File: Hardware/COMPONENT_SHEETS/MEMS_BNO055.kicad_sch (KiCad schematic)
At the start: 6 parts, among them U8 BNO055, Y2 32.768kHz

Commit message: Added 3D models to components
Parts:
- Y2: footprint Crystal:Crystal_DS26_D2.0mm_L6.0mm_Horizontal_1EP_style2 -> RDT_Custom_Footprints:XTAL_ABM7-32.000MHZ-D2Y-T
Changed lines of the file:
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@@
       (effects (font (size 1.27 1.27)) (justify left))
     )
-    (property "Footprint" "Crystal:Crystal_DS26_D2.0mm_L6.0mm_Horizontal_1EP_style2" (id 2) (at 163.83 83.82 0)
+    (property "Footprint" "RDT_Custom_Footprints:XTAL_ABM7-32.000MHZ-D2Y-T" (id 2) (at 163.83 83.82 0)
       (effects (font (size 1.27 1.27)) hide)
     )

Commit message: Corrected PCB edge cuts, removed components
Will be mimicking layout done by Seth Sievers
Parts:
- renumbered C19 to C1, C20 to C2, C21 to C3, C22 to C4, U8 to U1, Y2 to Y1
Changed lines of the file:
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@@
   (symbol (lib_id "Data_Collection_KiCAD_Project-rescue:BNO055-Sensor_Motion-Data_Collection_KiCAD_Project-rescue") (at 143.51 90.17 0)
     (in_bom yes) (on_board yes)
-    (property "Reference" "U8" (id 0) (at 143.51 63.5 0))
+    (property "Reference" "U1" (id 0) (at 143.51 63.5 0))
     (property "Value" "BNO055" (id 1) (at 143.51 66.04 0))
     (property "Footprint" "Package_LGA:LGA-28_5.2x3.8mm_P0.5mm" (id 2) (at 149.86 106.68 0)
@@
   (symbol (lib_id "Data_Collection_KiCAD_Project-rescue:+3.3V-power-Data_Collection_KiCAD_Project-rescue") (at 132.08 68.58 0)
     (in_bom yes) (on_board yes)
-    (property "Reference" "#PWR042" (id 0) (at 132.08 72.39 0)
+    (property "Reference" "#PWR013" (id 0) (at 132.08 72.39 0)
       (effects (font (size 1.27 1.27)) hide)
     )
@@
   (symbol (lib_id "Data_Collection_KiCAD_Project-rescue:GND-power-Data_Collection_KiCAD_Project-rescue") (at 162.56 69.85 0) (unit 1)
     (in_bom yes) (on_board yes)
-    (property "Reference" "#PWR0102" (id 0) (at 162.56 76.2 0)
+    (property "Reference" "#PWR015" (id 0) (at 162.56 76.2 0)
       (effects (font (size 1.27 1.27)) hide)
     )
@@
   (symbol (lib_id "Data_Collection_KiCAD_Project-rescue:GND-power-Data_Collection_KiCAD_Project-rescue") (at 140.97 110.49 0) (unit 1)
     (in_bom yes) (on_board yes)
-    (property "Reference" "#PWR0103" (id 0) (at 140.97 116.84 0)
+    (property "Reference" "#PWR014" (id 0) (at 140.97 116.84 0)
       (effects (font (size 1.27 1.27)) hide)
     )
@@
   (symbol (lib_id "Data_Collection_KiCAD_Project-rescue:Crystal_Small-Device-Data_Collection_KiCAD_Project-rescue") (at 163.83 83.82 270) (unit 1)
     (in_bom yes) (on_board yes)
-    (property "Reference" "Y2" (id 0) (at 166.0652 82.6516 90)
+    (property "Reference" "Y1" (id 0) (at 166.0652 82.6516 90)
       (effects (font (size 1.27 1.27)) (justify left))
     )
@@
   (symbol (lib_id "Data_Collection_KiCAD_Project-rescue:C_Small-Device-Data_Collection_KiCAD_Project-rescue") (at 160.02 68.58 270)
     (in_bom yes) (on_board yes)
-    (property "Reference" "C19" (id 0) (at 160.02 62.7634 90))
+    (property "Reference" "C1" (id 0) (at 160.02 62.7634 90))
     (property "Value" "0.1uF" (id 1) (at 160.02 65.0748 90))
     (property "Footprint" "Capacitor_SMD:C_0603_1608Metric_Pad1.08x0.95mm_HandSolder" (id 2) (at 160.02 68.58 0)
@@
   (symbol (lib_id "Data_Collection_KiCAD_Project-rescue:C_Small-Device-Data_Collection_KiCAD_Project-rescue") (at 171.45 77.47 270)
     (in_bom yes) (on_board yes)
-    (property "Reference" "C21" (id 0) (at 171.45 71.6534 90))
+    (property "Reference" "C3" (id 0) (at 171.45 71.6534 90))
     (property "Value" "0.1uF" (id 1) (at 171.45 73.9648 90))
     (property "Footprint" "Capacitor_SMD:C_0603_1608Metric_Pad1.08x0.95mm_HandSolder" (id 2) (at 171.45 77.47 0)
@@
   (symbol (lib_id "Data_Collection_KiCAD_Project-rescue:C_Small-Device-Data_Collection_KiCAD_Project-rescue") (at 171.45 90.17 270)
     (in_bom yes) (on_board yes)
-    (property "Reference" "C22" (id 0) (at 171.45 92.71 90))
+    (property "Reference" "C4" (id 0) (at 171.45 92.71 90))
     (property "Value" "0.1uF" (id 1) (at 171.45 95.25 90))
     (property "Footprint" "Capacitor_SMD:C_0603_1608Metric_Pad1.08x0.95mm_HandSolder" (id 2) (at 171.45 90.17 0)
@@
   (symbol (lib_id "Data_Collection_KiCAD_Project-rescue:GND-power-Data_Collection_KiCAD_Project-rescue") (at 180.34 90.17 0) (unit 1)
     (in_bom yes) (on_board yes)
-    (property "Reference" "#PWR0104" (id 0) (at 180.34 96.52 0)
+    (property "Reference" "#PWR017" (id 0) (at 180.34 96.52 0)
       (effects (font (size 1.27 1.27)) hide)
     )
@@
   (symbol (lib_id "Data_Collection_KiCAD_Project-rescue:GND-power-Data_Collection_KiCAD_Project-rescue") (at 123.19 104.14 0) (unit 1)
     (in_bom yes) (on_board yes)
-    (property "Reference" "#PWR0105" (id 0) (at 123.19 110.49 0)
+    (property "Reference" "#PWR012" (id 0) (at 123.19 110.49 0)
       (effects (font (size 1.27 1.27)) hide)
     )
@@
   (symbol (lib_id "Data_Collection_KiCAD_Project-rescue:GND-power-Data_Collection_KiCAD_Project-rescue") (at 170.18 110.49 0) (unit 1)
     (in_bom yes) (on_board yes)
-    (property "Reference" "#PWR0106" (id 0) (at 170.18 116.84 0)
+    (property "Reference" "#PWR016" (id 0) (at 170.18 116.84 0)
       (effects (font (size 1.27 1.27)) hide)
     )
@@
   (symbol (lib_id "Data_Collection_KiCAD_Project-rescue:C_Small-Device-Data_Collection_KiCAD_Project-rescue") (at 163.83 102.87 270)
     (in_bom yes) (on_board yes)
-    (property "Reference" "C20" (id 0) (at 163.83 105.41 90))
+    (property "Reference" "C2" (id 0) (at 163.83 105.41 90))
     (property "Value" "0.1uF" (id 1) (at 163.83 107.95 90))
     (property "Footprint" "Capacitor_SMD:C_0603_1608Metric_Pad1.08x0.95mm_HandSolder" (id 2) (at 163.83 102.87 0)

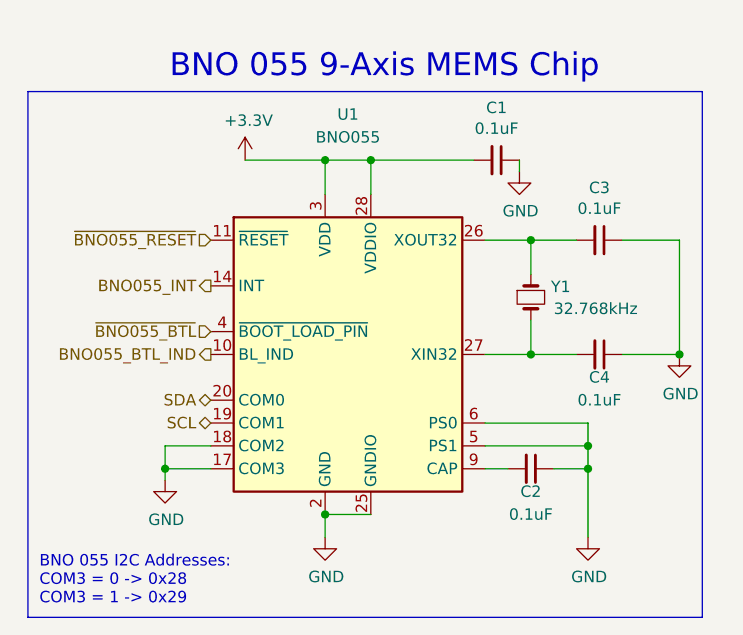
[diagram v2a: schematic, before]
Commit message: Organized components, arranged filter caps
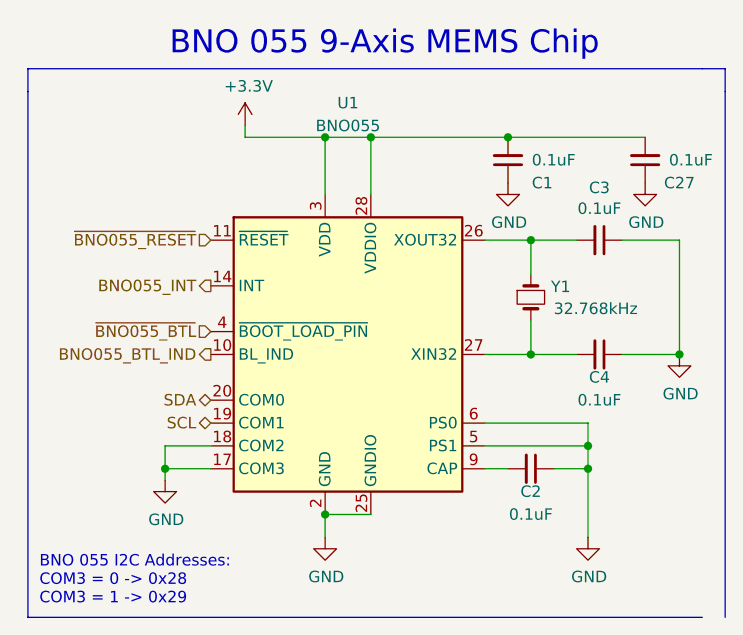
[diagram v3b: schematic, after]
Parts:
- added C27: 0.1uF, Capacitor_SMD:C_0603_1608Metric_Pad1.08x0.95mm_HandSolder, symbol Data_Collection_KiCAD_Project-rescue:C_Small-Device-Data_Collection_KiCAD_Proje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
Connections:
- net +3V3: now also C27.2
- net GND: now also C27.1
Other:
- moved on the sheet: C1
